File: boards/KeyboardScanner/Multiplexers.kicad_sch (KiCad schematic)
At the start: 16 parts, among them U1 74LS151, U10 74LS151, U2 74LS151, U3 74LS151, U4 74LS151, U6 74LS151, U7 74LS151, U9 74LS151

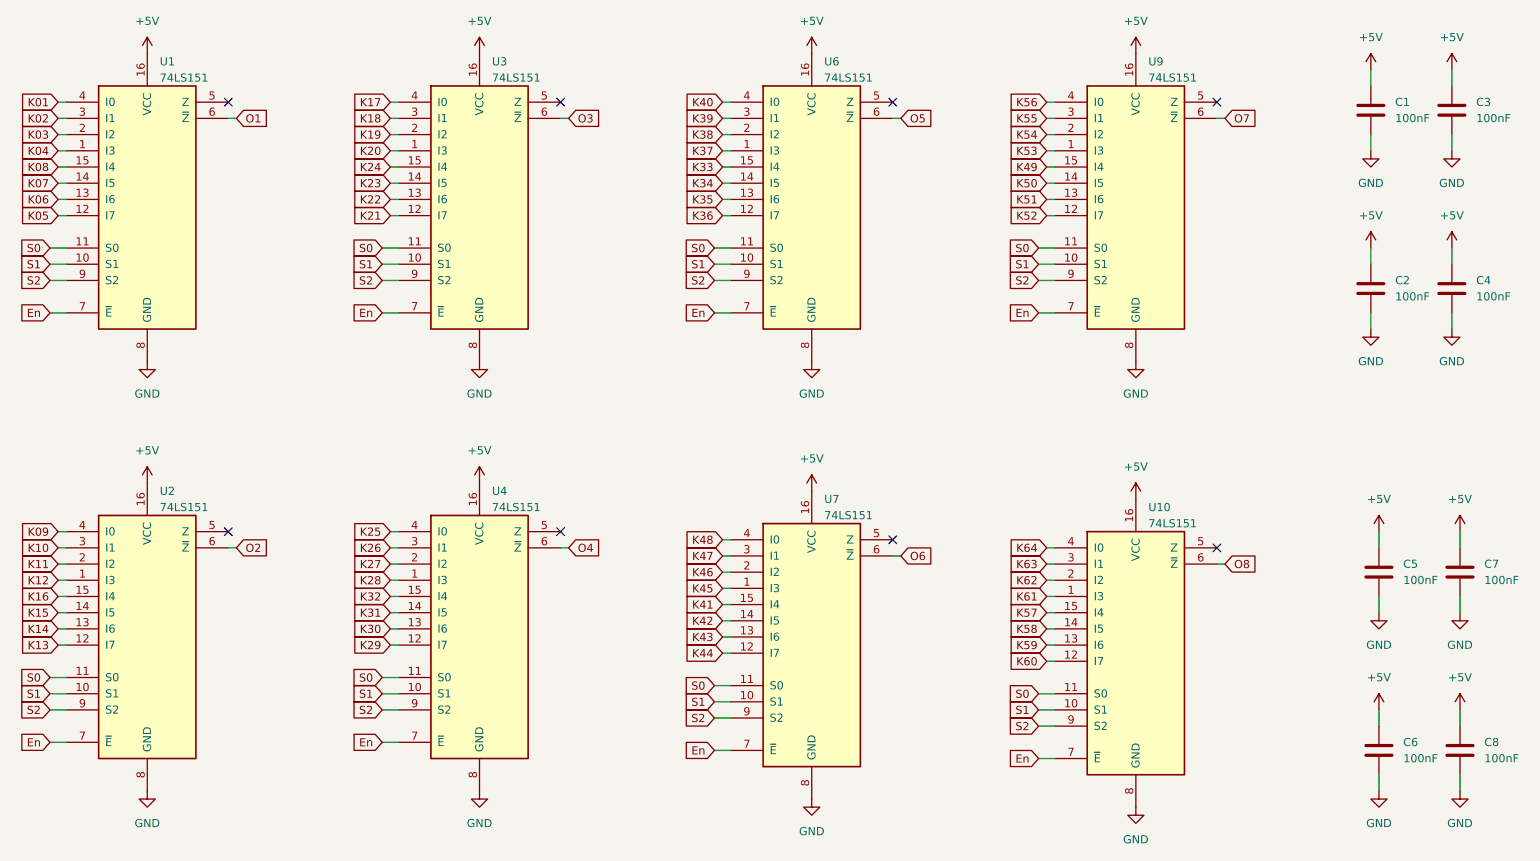
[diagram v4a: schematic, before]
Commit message: Revert "Reverting to using 2803A inverted open collector for Keyboard Scanner, fixed layout"
This reverts commit 7b46a6886eac97662925cbadd02de0ff96663bd2.
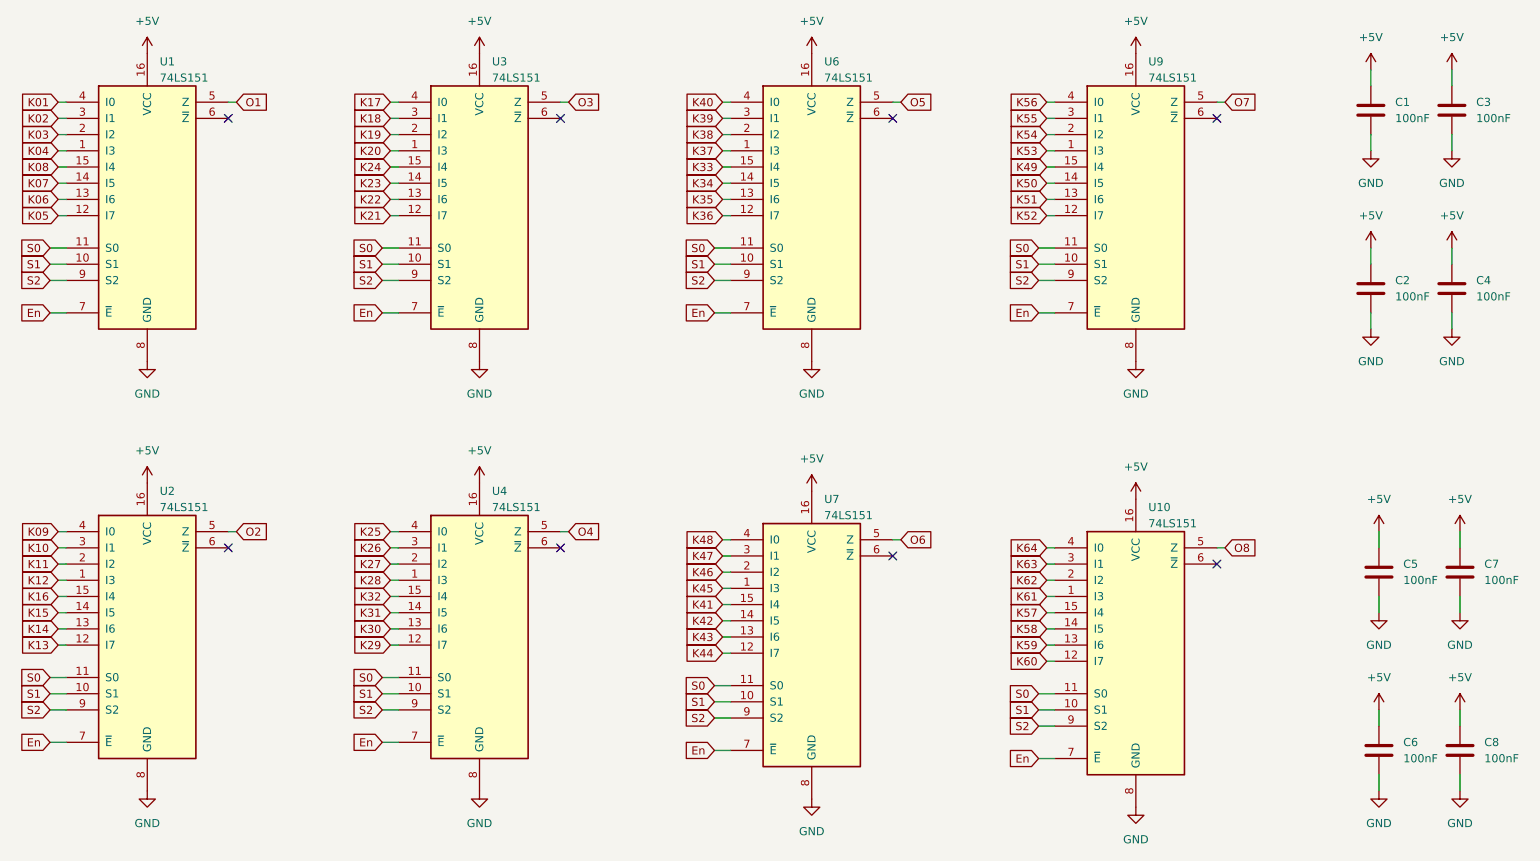
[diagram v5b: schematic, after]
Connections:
- net O1: now also U1.5 (Z); no longer U1.6 (~{Z})
- net O2: now also U2.5 (Z); no longer U2.6 (~{Z})
- net O3: now also U3.5 (Z); no longer U3.6 (~{Z})
- net O4: now also U4.5 (Z); no longer U4.6 (~{Z})
- net O5: now also U6.5 (Z); no longer U6.6 (~{Z})
- net O6: now also U7.5 (Z); no longer U7.6 (~{Z})
- net O7: now also U9.5 (Z); no longer U9.6 (~{Z})
- net O8: now also U10.5 (Z); no longer U10.6 (~{Z})
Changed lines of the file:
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@@
 	(paper "A4")
 	(no_connect
-		(at 66.04 39.37)
+		(at 66.04 41.91)
 	)
 	(no_connect
-		(at 170.18 39.37)
+		(at 170.18 41.91)
 	)
 	(no_connect
-		(at 170.18 107.95)
+		(at 170.18 110.49)
 	)
 	(no_connect
-		(at 118.11 39.37)
+		(at 118.11 41.91)
 	)
 	(no_connect
-		(at 220.98 39.37)
+		(at 220.98 41.91)
 	)
 	(no_connect
-		(at 220.98 109.22)
+		(at 220.98 111.76)
 	)
 	(no_connect
-		(at 66.04 106.68)
+		(at 66.04 109.22)
 	)
 	(no_connect
-		(at 118.11 106.68)
+		(at 118.11 109.22)
 	)
 	(wire
@@
 	(wire
 		(pts
-			(xy 170.18 110.49) (xy 171.45 110.49)
-		)
-		(stroke
-			(width 0)
-			(type default)
-		)
-	)
-	(wire
-		(pts
-			(xy 118.11 41.91) (xy 119.38 41.91)
+			(xy 170.18 107.95) (xy 171.45 107.95)
 		)
 		(stroke
@@
 	(wire
 		(pts
-			(xy 66.04 41.91) (xy 67.31 41.91)
+			(xy 66.04 39.37) (xy 67.31 39.37)
 		)
 		(stroke
@@
 	(wire
 		(pts
-			(xy 66.04 109.22) (xy 67.31 109.22)
+			(xy 66.04 106.68) (xy 67.31 106.68)
 		)
 		(stroke
@@
 	(wire
 		(pts
-			(xy 220.98 111.76) (xy 222.25 111.76)
+			(xy 220.98 109.22) (xy 222.25 109.22)
 		)
 		(stroke
@@
 	(wire
 		(pts
+			(xy 118.11 39.37) (xy 119.38 39.37)
+		)
+		(stroke
+			(width 0)
+			(type default)
+		)
+	)
+	(wire
+		(pts
 			(xy 91.44 39.37) (xy 92.71 39.37)
 		)
@@
 	(wire
 		(pts
-			(xy 220.98 41.91) (xy 222.25 41.91)
+			(xy 220.98 39.37) (xy 222.25 39.37)
 		)
 		(stroke
@@
 	(wire
 		(pts
-			(xy 118.11 109.22) (xy 119.38 109.22)
+			(xy 118.11 106.68) (xy 119.38 106.68)
 		)
 		(stroke
@@
 	(wire
 		(pts
-			(xy 170.18 41.91) (xy 171.45 41.91)
+			(xy 170.18 39.37) (xy 171.45 39.37)
 		)
 		(stroke
@@
 	(global_label "O1"
 		(shape input)
-		(at 67.31 41.91 0)
+		(at 67.31 39.37 0)
 		(fields_autoplaced yes)
 		(effects
@@
 		)
 		(property "Intersheetrefs" "${INTERSHEET_REFS}"
-			(at 72.2631 41.8306 0)
+			(at 72.2631 39.2906 0)
 			(effects
 				(font
@@
 	(global_label "O5"
 		(shape input)
-		(at 171.45 41.91 0)
+		(at 171.45 39.37 0)
 		(fields_autoplaced yes)
 		(effects
@@
 		)
 		(property "Intersheetrefs" "${INTERSHEET_REFS}"
-			(at 176.4031 41.8306 0)
+			(at 176.4031 39.2906 0)
 			(effects
 				(font
@@
 	(global_label "O4"
 		(shape input)
-		(at 119.38 109.22 0)
+		(at 119.38 106.68 0)
 		(fields_autoplaced yes)
 		(effects
@@
 		)
 		(property "Intersheetrefs" "${INTERSHEET_REFS}"
-			(at 124.3331 109.1406 0)
+			(at 124.3331 106.6006 0)
 			(effects
 				(font
@@
 	(global_label "O6"
 		(shape input)
-		(at 171.45 110.49 0)
+		(at 171.45 107.95 0)
 		(fields_autoplaced yes)
 		(effects
@@
 		)
 		(property "Intersheetrefs" "${INTERSHEET_REFS}"
-			(at 176.4031 110.4106 0)
+			(at 176.4031 107.8706 0)
 			(effects
 				(font
@@
 	(global_label "O7"
 		(shape input)
-		(at 222.25 41.91 0)
+		(at 222.25 39.37 0)
 		(fields_autoplaced yes)
 		(effects
@@
 		)
 		(property "Intersheetrefs" "${INTERSHEET_REFS}"
-			(at 227.2031 41.8306 0)
+			(at 227.2031 39.2906 0)
 			(effects
 				(font
@@
 	(global_label "O3"
 		(shape input)
-		(at 119.38 41.91 0)
+		(at 119.38 39.37 0)
 		(fields_autoplaced yes)
 		(effects
@@
 		)
 		(property "Intersheetrefs" "${INTERSHEET_REFS}"
-			(at 124.3331 41.8306 0)
+			(at 124.3331 39.2906 0)
 			(effects
 				(font
@@
 	(global_label "O2"
 		(shape input)
-		(at 67.31 109.22 0)
+		(at 67.31 106.68 0)
 		(fields_autoplaced yes)
 		(effects
@@
 		)
 		(property "Intersheetrefs" "${INTERSHEET_REFS}"
-			(at 72.2631 109.1406 0)
+			(at 72.2631 106.6006 0)
 			(effects
 				(font
@@
 	(global_label "O8"
 		(shape input)
-		(at 222.25 111.76 0)
+		(at 222.25 109.22 0)
 		(fields_autoplaced yes)
 		(effects
@@
 		)
 		(property "Intersheetrefs" "${INTERSHEET_REFS}"
-			(at 227.2031 111.6806 0)
-			(effects
-				(font
+			(at 227.2031 109.1406 0)
+			(effects
+				(font
